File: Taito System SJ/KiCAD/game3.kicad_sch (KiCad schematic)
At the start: 5 parts, among them U63 AY-3-8910 (AY_0)

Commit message: Added first 3 sound chips
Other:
- company: (none) -> ANTON GALE
- title: (none) -> TAITO SYSTEM SJ
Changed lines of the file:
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@@
 (kicad_sch (version 20211123) (generator eeschema)
   (paper "A4")
+  (title_block
+    (title "TAITO SYSTEM SJ")
+    (company "ANTON GALE")
+  )
   (junction (at 229.87 113.03) (diameter 0) (color 0 0 0 0)
   )

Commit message: IO Interface
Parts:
- added C? (x3): .01uF, symbol Device:C_Polarized_Small
- added C? (x3): .1uF, symbol Device:C_Polarized_Small
- added DS.A: SW_DIP_x08, symbol Switch:SW_DIP_x08
- added R?: 1K, symbol Device:R_US
- added R? (x6): 10K, symbol Device:R_US
- added RA?: 1k, Resistor_THT:R_Array_SIP9, symbol Device:R_Network08
- added TP?: PSG0, symbol Connector:TestPoint
- added U2, U7: 74LS257, symbol jt74:74LS257
- added U25, U26: 74LS367, symbol jt74:74LS367
- added U3, U4, U5, U6: 74LS253, symbol jt74:74LS253
- added U33: 74LS02, symbol jt74:74LS02
- added U43, U?: 74LS139, symbol jt74:74LS139
- added U53: 74LS04, symbol jt74:74LS04
- added U54: 74LS32, symbol jt74:74LS32
- RA? (x2): value 3.3k -> 1k
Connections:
- net GNDPWR: now also U63.24 (~{A9}), U63.3 (CHB), U63.38 (CHC), U63.4 (CHA), C?.1, C?.1, C?.1, DS.A.1, DS.A.2, DS.A.3, DS.A.4, DS.A.5, DS.A.6, DS.A.7, DS.A.8
- net VCC: now also R?.2, RA?.1 (common), U3.16 (VCC), U4.16 (VCC), U5.16 (VCC), U6.10 (I0b), U6.11 (I1b), U6.16 (VCC), U6.5 (I1a), U6.6 (I0a), U7.11 (I0d)
- net 1WAY OR 2WAY: now reaches DS.C.9, RA?.9 (R8), U63.13 (IOB0)
- net A1: now reaches U63.25 (A8)
- net A1: now also U3.2 (A1), U4.2 (A1), U5.2 (A1), U53.13, U54.1, U6.2 (A1)
- net BDIR: now reaches U63.27 (BDIR)
- net at U63.28 (BC2): now also R?.1
- net BC1: now reaches U63.29 (BC1)
- net AY_D0 renamed D0
- net D0: now also U25.7 (O3a)
- net AY_D1 renamed D1
- net D1: now also U25.5 (O2a)
- net AY_D2 renamed D2
- net D2: now also U25.3 (O1a)
- net AY_D3 renamed D3
- net D3: now also U26.13 (O6b)
- net AY_D4 renamed D4
- net D4: now also U26.11 (O5b)
- net AY_D5 renamed D5
- net D5: now also U25.13 (O6b)
- net AY_D6 renamed D6
- net D6: now also U25.11 (O5b)
- net AY_D7 renamed D7
- net D7: now also U25.9 (O4a)
- new net: C?.1, C?.2, R?.2 (x3)
- new net: C?.2, R?.1, R?.2 (x3)
- new net: U43.1 (E), U54.5, U54.8
- new net: U43.7 (O3), U54.2
- new net: U33.3, U?.9 (O3)
- new net: U33.1, U54.4
- new net A0: U2.1 (S), U3.14 (A0), U4.14 (A0), U5.14 (A0), U6.14 (A0), U7.1 (S)
- new net A2: U43.2 (A0), U?.14 (A0)
- new net A3: U43.3 (A1), U?.13 (A1)
- new net DP0: DS.A.16, RA?.2 (R1), U3.4 (I2a)
- new net DP1: DS.A.15, RA?.3 (R2), U3.12 (I2b)
- new net DP2: DS.A.14, RA?.4 (R3), U4.4 (I2a)
- new net DP3: DS.A.13, RA?.5 (R4), U4.12 (I2b)
- new net DP4: DS.A.12, RA?.6 (R5), U5.4 (I2a)
- new net DP5: DS.A.11, RA?.7 (R6), U5.12 (I2b)
- new net DP6: DS.A.10, RA?.8 (R7), U6.4 (I2a)
- new net DP7: DS.A.9, RA?.9 (R8), U6.12 (I2b)
- new net ED0: U2.4 (Za), U25.6 (I3)
- new net ED1: U2.7 (Zb), U25.4 (I2)
- new net ED2: U2.9 (Zc), U25.2 (I1), U4.7 (Za)
- new net ED3: U2.12 (Zd), U26.14 (I6), U4.9 (Zb)
- new net ED4: U26.12 (I5), U5.7 (Za), U7.4 (Za)
- new net ED5: U25.14 (I6), U5.9 (Zb), U7.7 (Zb)
- new net ED6: U25.12 (I5), U3.7 (Za), U6.7 (Za), U7.9 (Zc)
- new net ED7: U25.10 (I4), U3.9 (Zb), U6.9 (Zb), U7.12 (Zd)
- new net IN0: U3.6 (I0a)
- new net IN1: U3.10 (I0b)
- new net IN10: U3.5 (I1a)
- new net IN11: U3.11 (I1b)
- new net IN12: U4.5 (I1a)
- new net IN13: U4.11 (I1b)
- new net IN14: U5.5 (I1a)
- new net IN15: U5.11 (I1b)
- new net IN2: U4.6 (I0a)
- new net IN3: U4.10 (I0b)
- new net IN30: U3.3 (I3a)
- new net IN31: U3.13 (I3b)
- new net IN32: U4.3 (I3a)
- new net IN33: U4.13 (I3b)
- new net IN34: U5.3 (I3a)
- new net IN35: U5.13 (I3b)
- new net IN36: U6.3 (I3a)
- new net IN37: U6.13 (I3b)
- new net IN4: U5.6 (I0a)
- new net IN40: U2.2 (I0a)
- new net IN41: U2.5 (I0b)
- new net IN42: U2.14 (I0c)
- new net IN43: U2.11 (I0d)
- new net IN44: U7.2 (I0a)
- new net IN45: U7.5 (I0b)
- new net IN46: U7.14 (I0c)
- new net IN5: U5.10 (I0b)
- new net IN50: U2.3 (I1a)
- new net IN51: U2.6 (I1b)
- new net IN52: U2.13 (I1c)
- new net IN53: U2.10 (I1d)
- new net IN54: U7.3 (I1a)
- new net IN55: U7.6 (I1b)
- new net IN56: U7.13 (I1c)
- new net IN57: U7.10 (I1d)
- new net OUT0: R?.1, R?.1, R?.1, TP?.1
- new net READIN: U25.1 (OEa), U25.15 (OEb), U26.15 (OEb), U54.6
- new net VSS: U3.8 (VSS), U4.8 (VSS), U5.8 (VSS), U6.8 (VSS)
- new net ~{A1: U33.2, U53.12
- new net ~{EXRHR}: U43.5 (O1)
- new net ~{HTRRQ}: U43.4 (O0)
- new net ~{INPUT1}: U3.1 (OEa), U3.15 (OEb), U4.1 (OEa), U4.15 (OEb), U43.6 (O2), U5.1 (OEa), U5.15 (OEb), U6.1 (OEa), U6.15 (OEb)
- new net ~{INPUT2}: U2.15 (OE), U54.3, U7.15 (OE)
- new net ~{RD}: U54.10
- new net ~{READ}: U54.9, U?.15 (E)
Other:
- moved on the sheet: DS.B, DS.C, RA?, U63

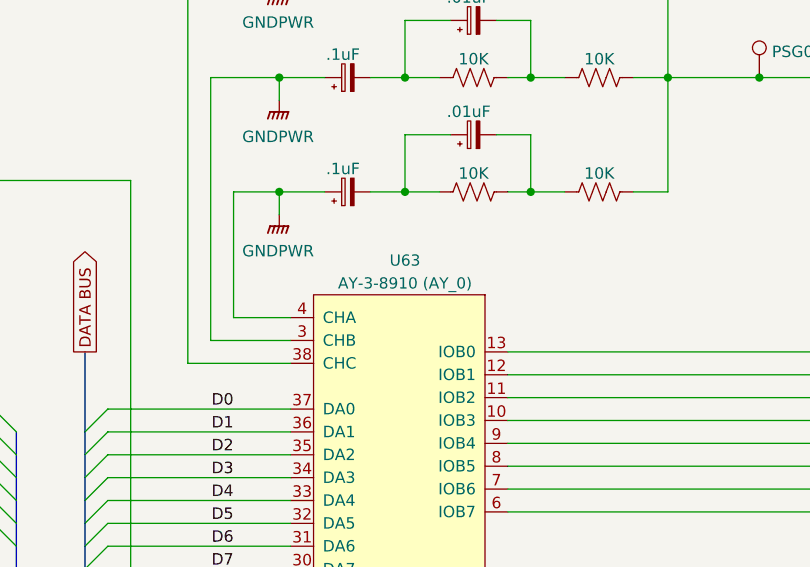
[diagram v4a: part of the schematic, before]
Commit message: Component naming updates
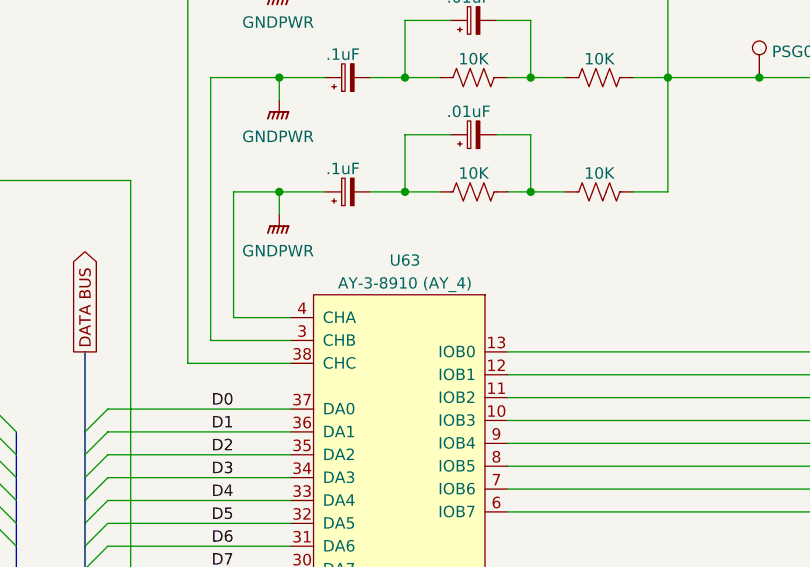
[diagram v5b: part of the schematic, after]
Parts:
- U63: value AY-3-8910 (AY_0) -> AY-3-8910 (AY_4)
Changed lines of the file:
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@@
       (effects (font (size 1.2446 1.2446)))
     )
-    (property "Value" "AY-3-8910 (AY_0)" (at 386.08 60.96 0)
+    (property "Value" "AY-3-8910 (AY_4)" (at 386.08 60.96 0)
       (effects (font (size 1.2446 1.2446)))
     )

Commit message: Tidied up loose ends
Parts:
- U63: value AY-3-8910 (AY_4) -> AY-3-8910 (AY_0)
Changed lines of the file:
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@@
       (effects (font (size 1.2446 1.2446)))
     )
-    (property "Value" "AY-3-8910 (AY_4)" (at 386.08 60.96 0)
+    (property "Value" "AY-3-8910 (AY_0)" (at 386.08 60.96 0)
       (effects (font (size 1.2446 1.2446)))
     )

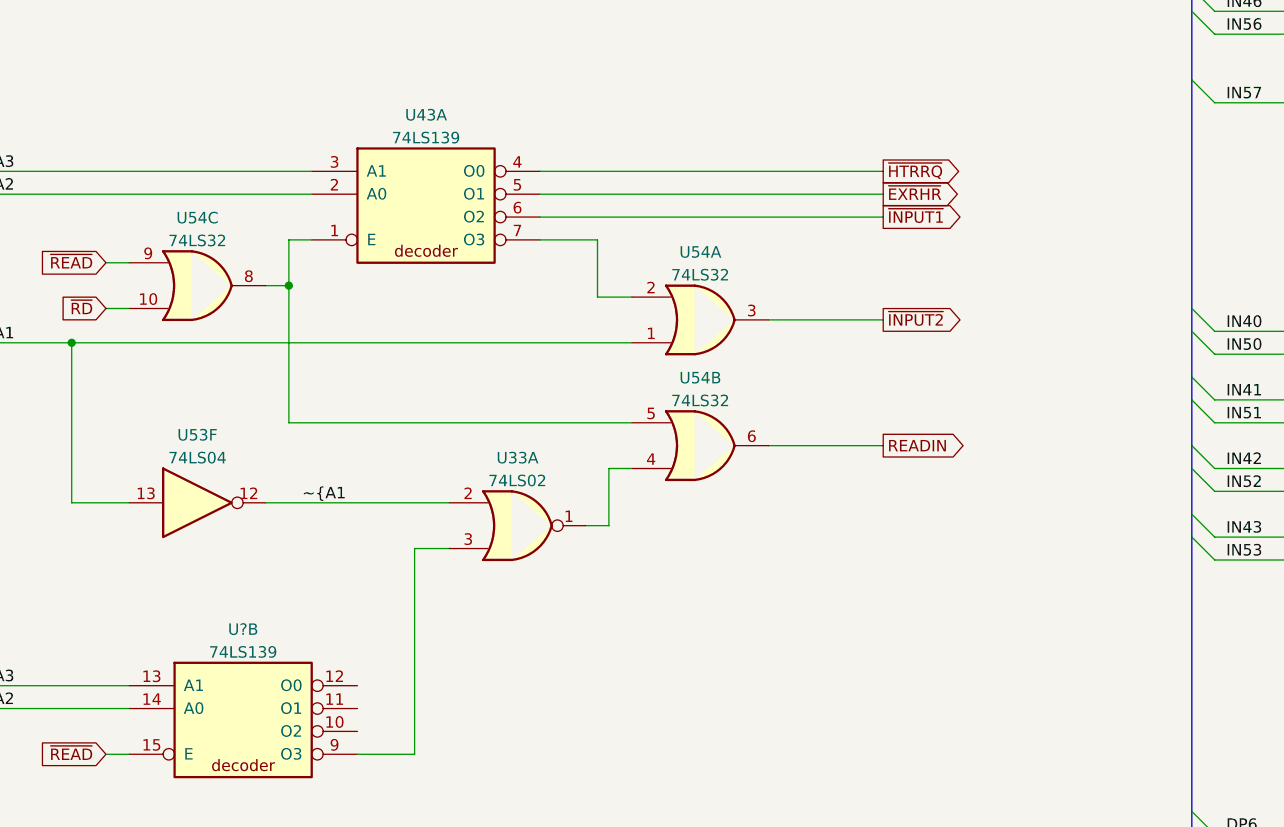
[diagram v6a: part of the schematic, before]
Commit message: Added MCU to Taito SJ Schematics
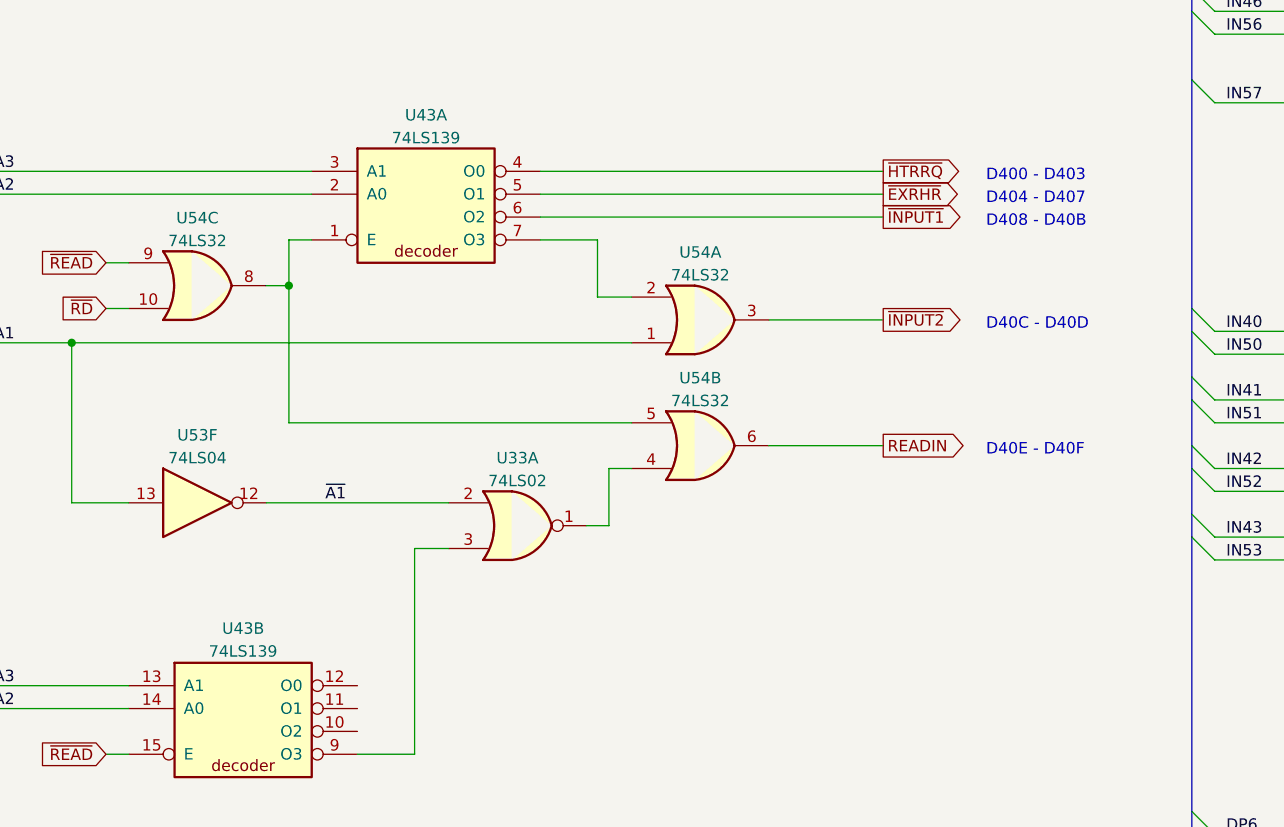
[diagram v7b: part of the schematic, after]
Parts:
- gave numbers to parts that had none: 1
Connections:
- net ~{A1 renamed ~{A1}
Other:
- note added: "D400 - D403"
- note added: "D404 - D407"
- note added: "D408 - D40B"
- note added: "D40C - D40D"
- note added: "D40E - D40F"
